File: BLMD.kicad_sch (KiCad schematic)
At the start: 34 parts, among them J1 CAN, J10 Conn_ST_STDC14, J2 CAN, J3 HALL, J4 ENCODER, J5 M2006, J6 USB_C_Receptacle_USB2.0_14P, J8 24V IN, J9 MOTOR, SW1 NRST, U10 CH340E, U11 STM32F303K8Tx, U12 BD41044FJ-C, U13 NJM12877, U15 L7812

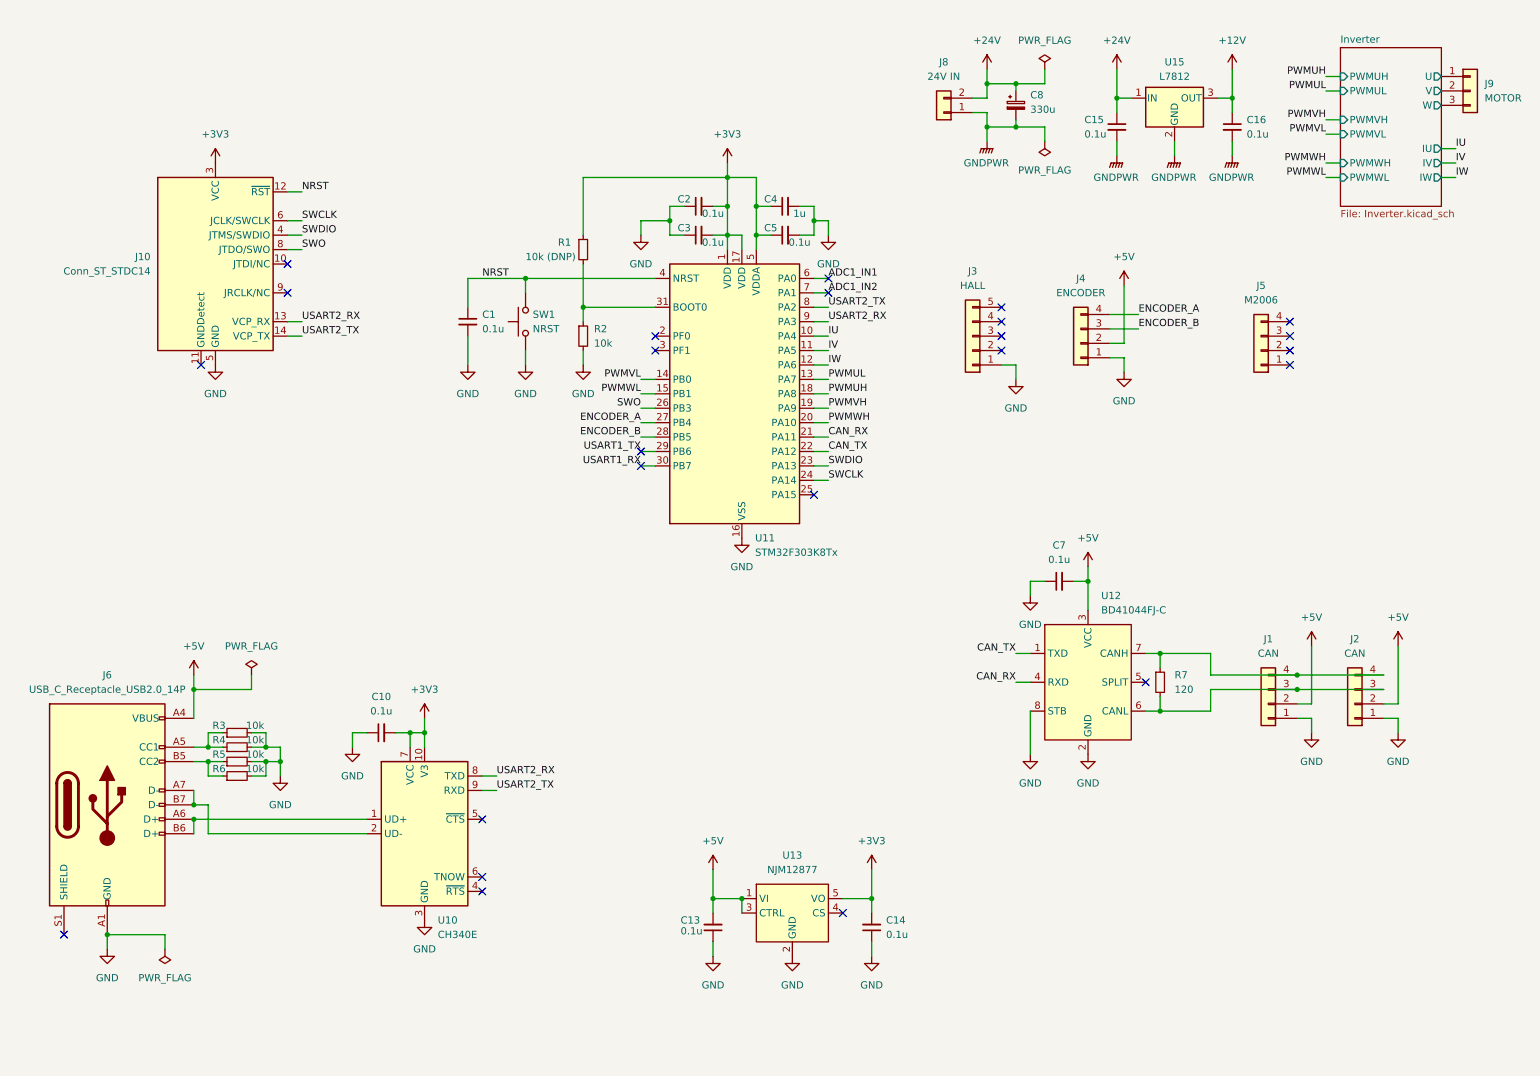
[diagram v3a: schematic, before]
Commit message: chore: Exclude power pin not driven errors in ERC
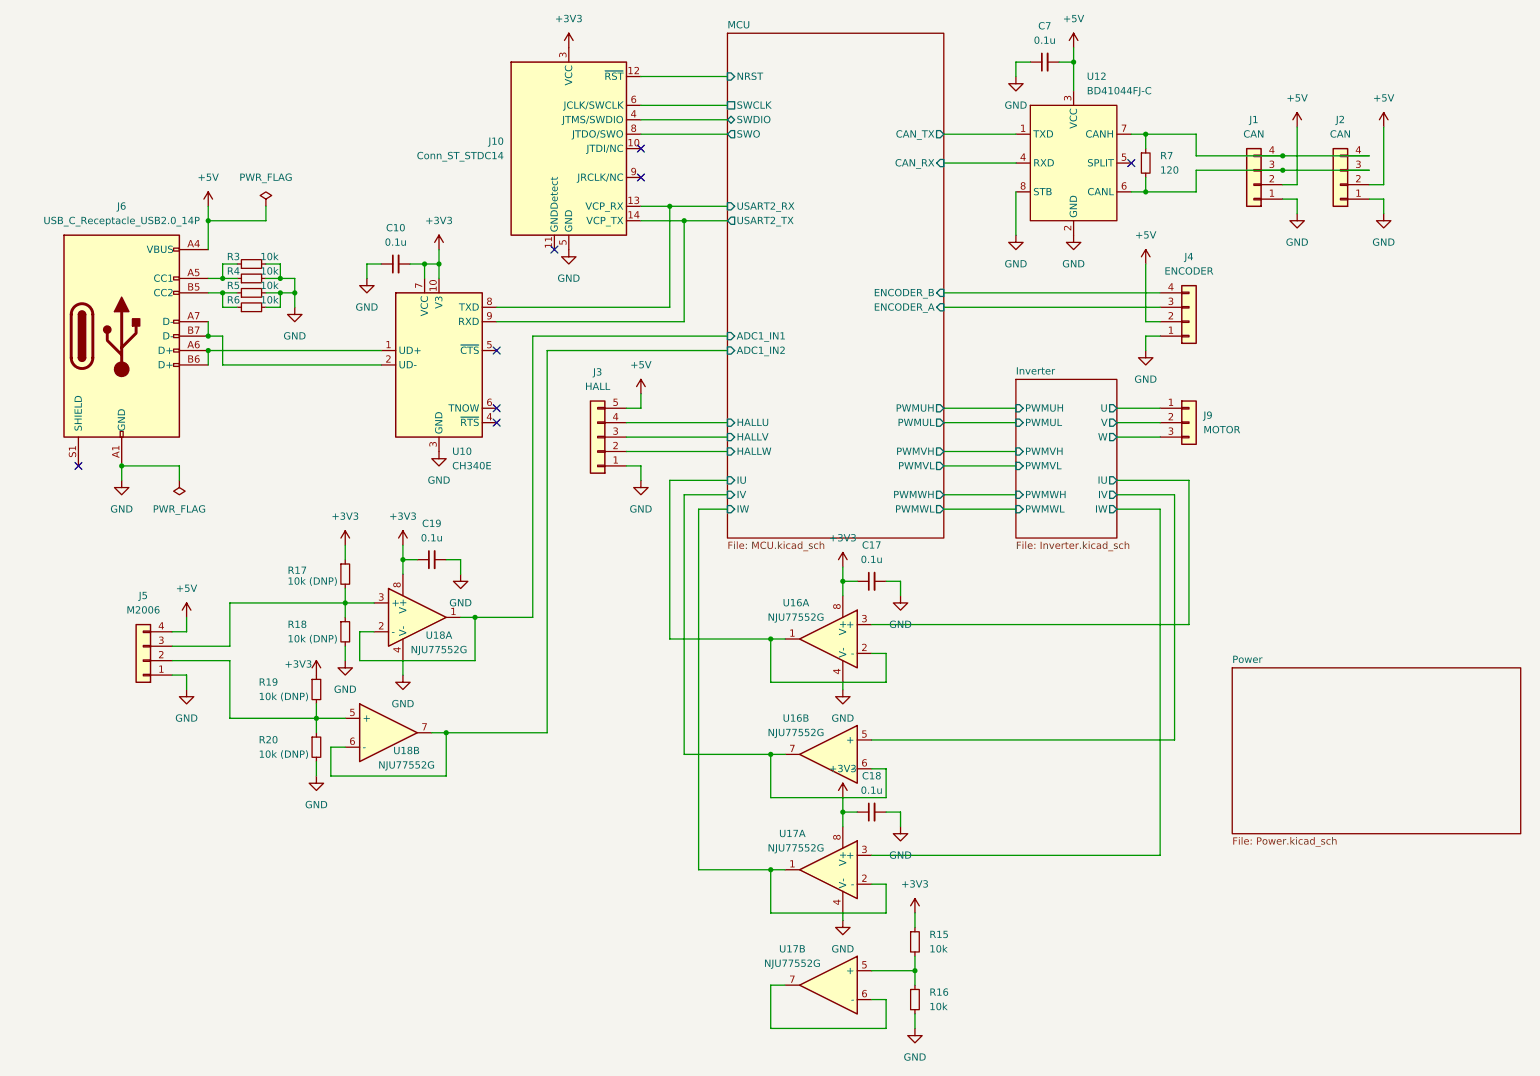
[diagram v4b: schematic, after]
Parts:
- removed C1, C13, C14, C15, C16, C2, C3, C5: 0.1u, Capacitor_SMD:C_0603_1608Metric_Pad1.08x0.95mm_HandSolder, symbol Device:C_Small
- removed C4: 1u, Capacitor_SMD:C_0603_1608Metric_Pad1.08x0.95mm_HandSolder, symbol Device:C_Small
- removed C8: 330u, Capacitor_SMD:CP_Elec_10x10.5, symbol Device:C_Polarized_Small
- removed J8: 24V IN, Connector_AMASS:AMASS_XT60PW-M_1x02_P7.20mm_Horizontal, symbol Connector_Generic:Conn_01x02
- removed R1: 10k (DNP), Resistor_SMD:R_0603_1608Metric_Pad0.98x0.95mm_HandSolder, symbol Device:R_Small
- removed R2: 10k, Resistor_SMD:R_0603_1608Metric_Pad0.98x0.95mm_HandSolder, symbol Device:R_Small
- removed SW1: NRST, Button_Switch_THT:SW_PUSH_1P1T_6x3.5mm_H4.3_APEM_MJTP1243, symbol Switch:SW_Push
- removed U11: STM32F303K8Tx, Package_QFP:LQFP-32_7x7mm_P0.8mm, symbol MCU_ST_STM32F3:STM32F303K8Tx
- removed U13: NJM12877, Package_TO_SOT_SMD:SOT-23-5_HandSoldering, symbol BLMD:NJM12877
- removed U15: L7812, Package_TO_SOT_THT:TO-220-3_Vertical, symbol Regulator_Linear:L7812
- added C17, C18, C19: 0.1u, Capacitor_SMD:C_0603_1608Metric_Pad1.08x0.95mm_HandSolder, symbol Device:C_Small
- added R15, R16: 10k, Resistor_SMD:R_0603_1608Metric_Pad0.98x0.95mm_HandSolder, symbol Device:R_Small
- added R17, R18, R19, R20: 10k (DNP), Resistor_SMD:R_0603_1608Metric_Pad0.98x0.95mm_HandSolder, symbol Device:R_Small
- added U16, U17, U18: NJU77552G, Package_SO:SOP-8_3.9x4.9mm_P1.27mm, symbol Device:Opamp_Dual
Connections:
- net +3V3: now also C17.1, C18.1, C19.1, R15.1, R17.1, R19.1, U16.8 (V+), U17.8 (V+), U18.8 (V+)
- net +5V: now also J3.5 (Pin_5), J5.4 (Pin_4)
- net GND: now also J5.1 (Pin_1), C17.2, C18.2, C19.2, R16.2, R18.2, R20.2, U16.4 (V-), U17.4 (V-), U18.4 (V-)
- net at J5.2 (Pin_2): now also R19.2, R20.1, U18.5 (+)
- net at J5.3 (Pin_3): now also R17.2, R18.1, U18.3 (+)
- net MCU/HALLW: now reaches J3.2 (Pin_2)
- net MCU/HALLV: now reaches J3.3 (Pin_3)
- net MCU/HALLU: now reaches J3.4 (Pin_4)
- net CAN_RX renamed MCU/CAN_RX
- net CAN_TX renamed MCU/CAN_TX
- net ENCODER_A renamed MCU/ENCODER_B
- net ENCODER_B renamed MCU/ENCODER_A
- net NRST renamed MCU/NRST
- net SWCLK renamed MCU/SWCLK
- net SWDIO renamed MCU/SWDIO
- net SWO renamed MCU/SWO
- net USART2_RX renamed MCU/USART2_RX
- net USART2_TX renamed MCU/USART2_TX
- new net: R15.2, R16.1, U17.5 (+)
- new net: U17.6 (-), U17.7
- new net Inverter/IU: U16.3 (+)
- new net Inverter/IV: U16.5 (+)
- new net Inverter/IW: U17.3 (+)
- new net MCU/ADC1_IN1: U18.1, U18.2 (-)
- new net MCU/ADC1_IN2: U18.6 (-), U18.7
- new net MCU/IU: U16.1, U16.2 (-)
- new net MCU/IV: U16.6 (-), U16.7
- new net MCU/IW: U17.1, U17.2 (-)
- no-connect marks 24 -> 8
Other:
- added sheet MCU (MCU.kicad_sch)
- added sheet Power (Power.kicad_sch)
- moved on the sheet: C10, C7, J1, J10, J2, J3, J4, J5, J6, J9, R3, R4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
